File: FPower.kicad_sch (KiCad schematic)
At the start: 48 parts, among them IC1 TSS721, J2 CONMHF1-SMD-G-T, J3 USB4520-03-0-A_REVA, J4 54602-908LF, SW2 SW_Push, SW3 SW_Push, U1 ESP32-C3, U2 W25Q16JVSS, U3 USBLC6-2SC6, U4 TPS2116DRL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

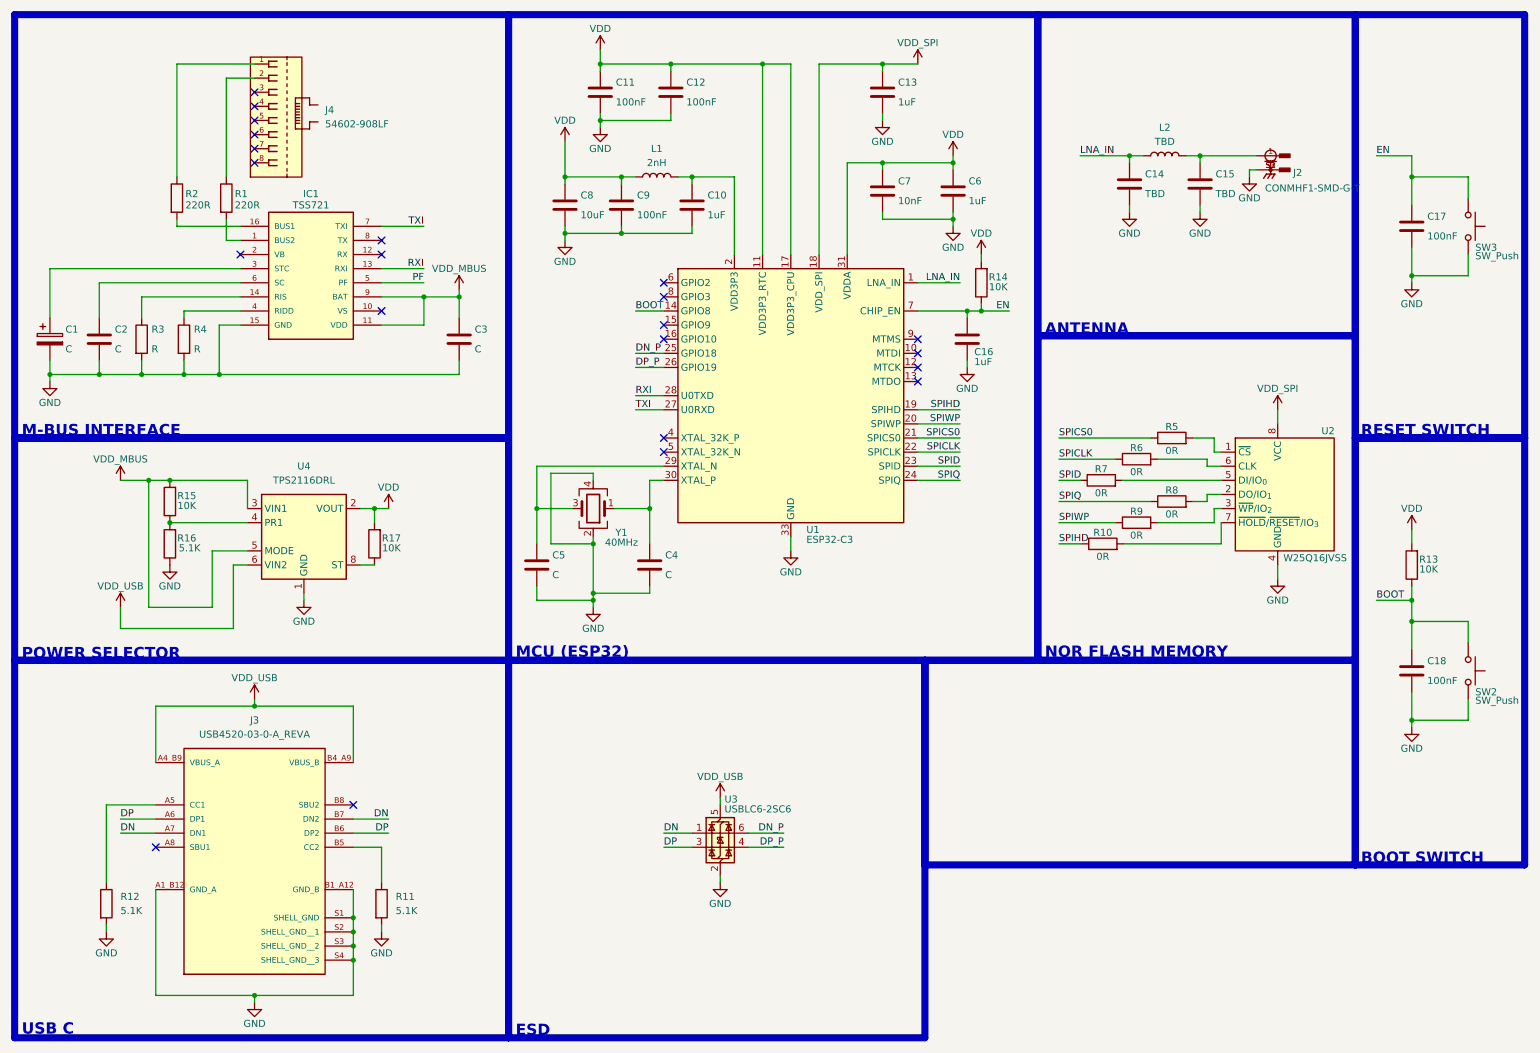
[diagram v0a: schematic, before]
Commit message: updated component values
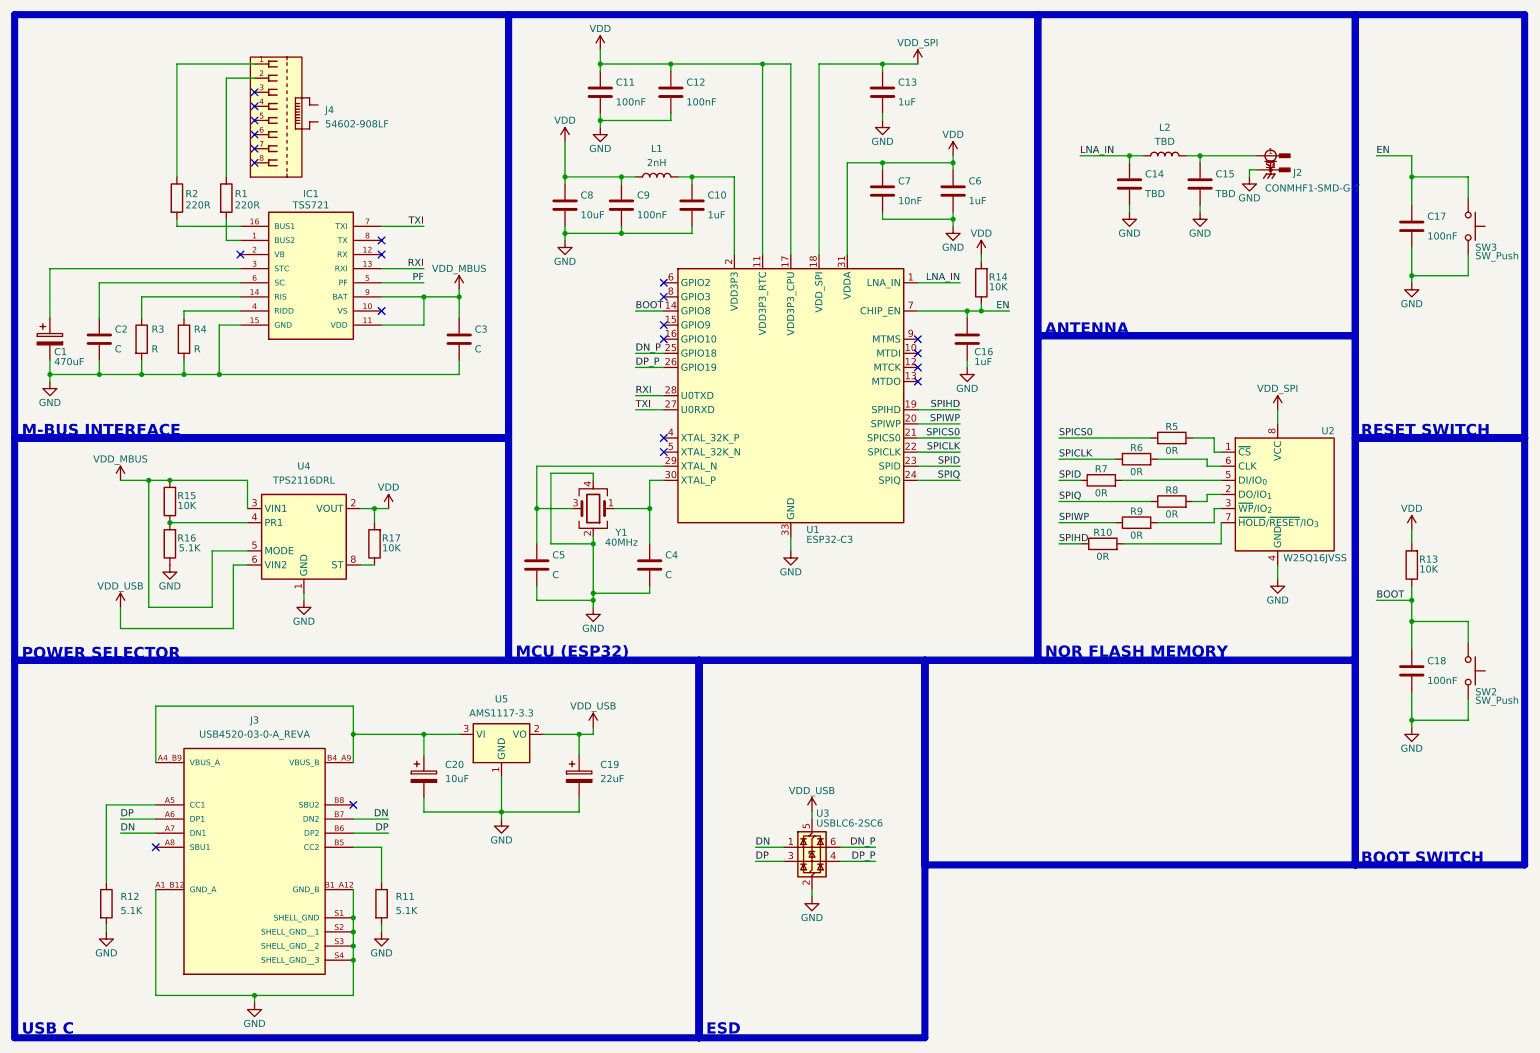
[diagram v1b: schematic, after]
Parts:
- added C19: 22uF, symbol Device:C_Polarized
- added C20: 10uF, symbol Device:C_Polarized
- added U5: AMS1117-3.3, Package_TO_SOT_SMD:SOT-223-3_TabPin2, symbol Regulator_Linear:AMS1117-3.3
- C1: value C -> 470uF
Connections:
- net GND: now also C19.2, C20.2, U5.1 (GND)
- net VDD_USB: now also C19.1, U5.2 (VO); no longer J3.A4_B9 (VBUS_A), J3.B4_A9 (VBUS_B)
- new net: C20.1, J3.A4_B9 (VBUS_A), J3.B4_A9 (VBUS_B), U5.3 (VI)
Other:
- moved on the sheet: U3
